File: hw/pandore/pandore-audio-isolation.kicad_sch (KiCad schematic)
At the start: 15 parts, among them U23 ISO7762, U24 ISO1640

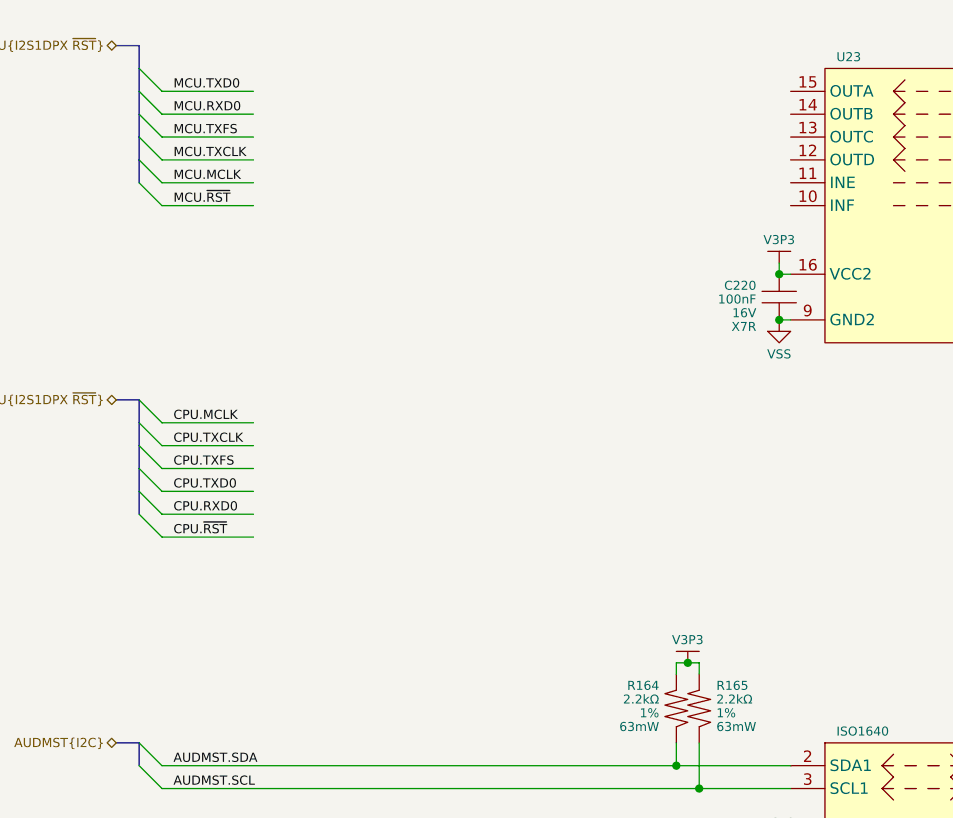
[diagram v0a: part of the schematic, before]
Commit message: lots of routing (diff, buses, power) done optimised buffer out
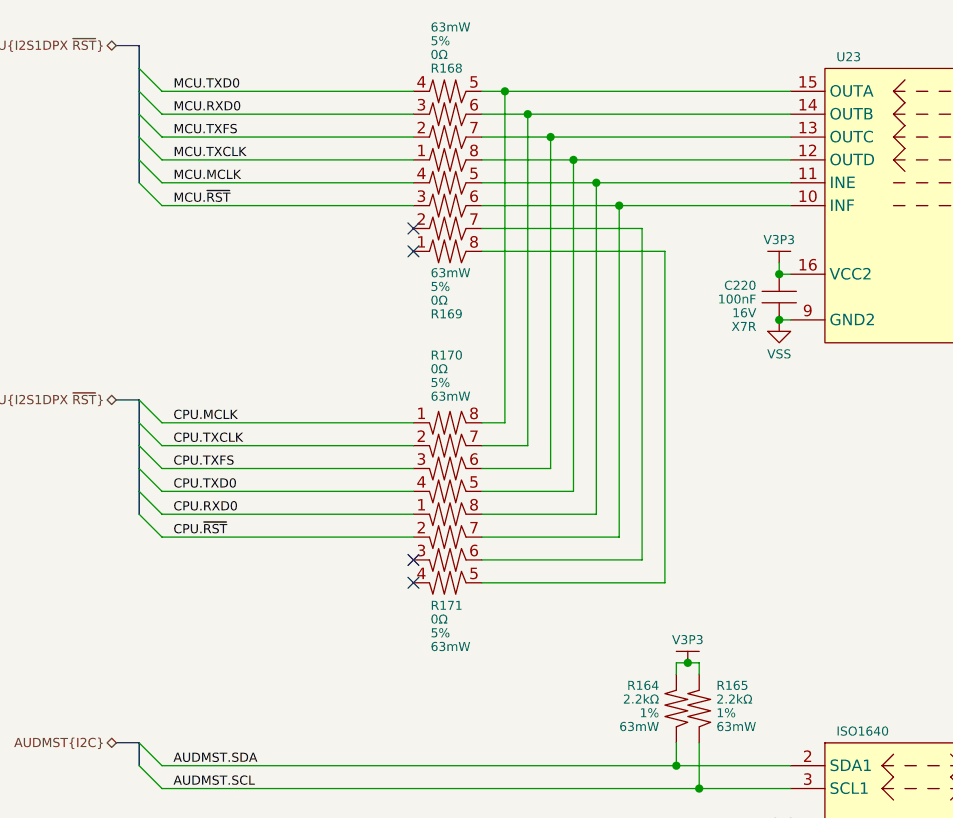
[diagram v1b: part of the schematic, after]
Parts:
- added R168, R169, R170, R171: ${Resistance}, ${Tolerance}, ${Power}, reekilib_res:RESCAXSR50P200X100X35-8, symbol reekilib_res:res_4
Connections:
- net CPU.MCLK: now also R170.1
- net CPU.RXD0: now also R171.1
- net CPU.TXCLK: now also R170.2
- net CPU.TXD0: now also R170.4
- net CPU.TXFS: now also R170.3
- net CPU.~{RST}: now also R171.2
- net MCU.MCLK: now also R169.4
- net MCU.RXD0: now also R168.3
- net MCU.TXCLK: now also R168.1
- net MCU.TXD0: now also R168.4
- net MCU.TXFS: now also R168.2
- net MCU.~{RST}: now also R169.3
- net at U23.10 (INF): now also R169.6, R171.7
- net at U23.11 (INE): now also R169.5, R171.8
- net at U23.12 (OUTD): now also R168.8, R170.5
- net at U23.13 (OUTC): now also R168.7, R170.6
- net at U23.14 (OUTB): now also R168.6, R170.7
- net at U23.15 (OUTA): now also R168.5, R170.8
- new net: R169.7, R171.6
- new net: R169.8, R171.5
- no-connect marks 0 -> 4

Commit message: added todos following review
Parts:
- R170, R171: now not fitted
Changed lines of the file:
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@@
 		(in_bom yes)
 		(on_board yes)
-		(dnp no)
+		(dnp yes)
 		(property "Reference" "R171"
 			(at 80.645 105.41 90)
@@
 		(in_bom yes)
 		(on_board yes)
-		(dnp no)
+		(dnp yes)
 		(property "Reference" "R170"
 			(at 80.645 77.597 90)

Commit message: added expansion port and more ctl to rp2350s routing much progress
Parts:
- added EXP8: I2C, reekilib_con:HDR254P1X02-TH, symbol reekilib_con:hdr-1x2
- added EXP9: I2S, reekilib_con:HDR254P1X08-TH, symbol reekilib_con:hdr-1x8
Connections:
- net AV3P3: now also EXP9.1
- net CODEC.MCLK: now also EXP9.5
- net CODEC.RXD0: now also EXP9.2
- net CODEC.SCL: now also EXP8.1
- net CODEC.SDA: now also EXP8.2
- net CODEC.TXCLK: now also EXP9.3
- net CODEC.TXD0: now also EXP9.6
- net CODEC.TXFS: now also EXP9.4
- net VSSISO: now also EXP9.8
- net ~{RST}: now also EXP9.7

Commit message: more routing/placement done added 5v load switch 1A each added second fan circuit redone all diffpair routing following new stackup calc added all (?) missing connectors to unused pins
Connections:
- net V3P3 renamed V3P3AUD
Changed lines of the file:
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@@
 	)
 	(junction
+		(at 109.22 111.76)
+		(diameter 0)
+		(color 0 0 0 0)
+	)
+	(junction
 		(at 107.95 123.19)
 		(diameter 0)
@@
 	)
 	(junction
-		(at 109.22 111.76)
-		(diameter 0)
-		(color 0 0 0 0)
-	)
-	(junction
 		(at 110.49 125.73)
 		(diameter 0)
@@
 	(wire
 		(pts
-			(xy 110.49 111.76) (xy 109.22 111.76)
+			(xy 162.56 50.8) (xy 184.15 50.8)
 		)
 		(stroke
@@
 	(wire
 		(pts
-			(xy 162.56 50.8) (xy 184.15 50.8)
+			(xy 201.93 48.26) (xy 214.63 48.26)
 		)
 		(stroke
@@
 	(wire
 		(pts
-			(xy 201.93 48.26) (xy 214.63 48.26)
+			(xy 109.22 111.76) (xy 110.49 111.76)
 		)
 		(stroke
@@
 	)
 	(symbol
+		(lib_id "reekilib_pwr:VDD")
+		(at 119.38 66.04 0)
+		(unit 1)
+		(exclude_from_sim no)
+		(in_bom no)
+		(on_board no)
+		(dnp no)
+		(property "Reference" "#PWR0243"
+			(at 119.38 62.865 0)
+			(do_not_autoplace yes)
+			(effects
+				(font
+					(size 1 1)
+				)
+				(hide yes)
+			)
+		)
+		(property "Value" "V3P3AUD"
+			(at 119.38 64.77 0)
+			(effects
+				(font
+					(size 1 1)
+				)
+			)
+		)
+		(property "Footprint" ""
+			(at 119.38 66.04 0)
+			(effects
+				(font
+					(size 1.524 1.524)
+				)
+			)
+		)
+		(property "Datasheet" ""
+			(at 119.38 66.04 0)
+			(effects
+				(font
+					(size 1.524 1.524)
+				)
+			)
+		)
+		(property "Description" ""
+			(at 119.38 66.04 0)
+			(effects
+				(font
+					(size 1.27 1.27)
+				)
+				(hide yes)
+			)
+		)
+		(pin "1"
+		)
+		(instances
+			(project "pandore"
+				(path "/e55f2700-f75a-4062-8a27-fe258faa8966/b4e2772d-7748-46ec-bd38-bc8e72cebcb8/07e56b51-9be1-414d-8c59-faa1629d64d5"
+					(reference "#PWR0243")
+					(unit 1)
+				)
+			)
+		)
+	)
+	(symbol
 		(lib_id "reekilib_cap:cap")
 		(at 119.38 135.89 0)
@@
 	)
 	(symbol
-		(lib_id "reekilib_pwr:VDD")
-		(at 119.38 130.81 0)
-		(unit 1)
-		(exclude_from_sim no)
-		(in_bom no)
-		(on_board no)
-		(dnp no)
-		(property "Reference" "#PWR0244"
-			(at 119.38 127.635 0)
-			(do_not_autoplace yes)
-			(effects
-				(font
-					(size 1 1)
-				)
-				(hide yes)
-			)
-		)
-		(property "Value" "V3P3"
-			(at 119.38 129.54 0)
-			(effects
-				(font
-					(size 1 1)
-				)
-			)
-		)
-		(property "Footprint" ""
-			(at 119.38 130.81 0)
-			(effects
-				(font
-					(size 1.524 1.524)
-				)
-			)
-		)
-		(property "Datasheet" ""
-			(at 119.38 130.81 0)
-			(effects
-				(font
-					(size 1.524 1.524)
-				)
-			)
-		)
-		(property "Description" ""
-			(at 119.38 130.81 0)
-			(effects
-				(font
-					(size 1.27 1.27)
-				)
-				(hide yes)
-			)
-		)
-		(pin "1"
-		)
-		(instances
-			(project "pandore"
-				(path "/e55f2700-f75a-4062-8a27-fe258faa8966/b4e2772d-7748-46ec-bd38-bc8e72cebcb8/07e56b51-9be1-414d-8c59-faa1629d64d5"
-					(reference "#PWR0244")
-					(unit 1)
-				)
-			)
-		)
-	)
-	(symbol
 		(lib_id "reekilib_res:res_4")
 		(at 82.55 88.9 90)
@@
 	)
 	(symbol
+		(lib_id "reekilib_pwr:VDD")
+		(at 109.22 110.49 0)
+		(unit 1)
+		(exclude_from_sim no)
+		(in_bom no)
+		(on_board no)
+		(dnp no)
+		(property "Reference" "#PWR0248"
+			(at 109.22 107.315 0)
+			(do_not_autoplace yes)
+			(effects
+				(font
+					(size 1 1)
+				)
+				(hide yes)
+			)
+		)
+		(property "Value" "V3P3AUD"
+			(at 109.22 109.22 0)
+			(effects
+				(font
+					(size 1 1)
+				)
+			)
+		)
+		(property "Footprint" ""
+			(at 109.22 110.49 0)
+			(effects
+				(font
+					(size 1.524 1.524)
+				)
+			)
+		)
+		(property "Datasheet" ""
+			(at 109.22 110.49 0)
+			(effects
+				(font
+					(size 1.524 1.524)
+				)
+			)
+		)
+		(property "Description" ""
+			(at 109.22 110.49 0)
+			(effects
+				(font
+					(size 1.27 1.27)
+				)
+				(hide yes)
+			)
+		)
+		(pin "1"
+		)
+		(instances
+			(project "pandore"
+				(path "/e55f2700-f75a-4062-8a27-fe258faa8966/b4e2772d-7748-46ec-bd38-bc8e72cebcb8/07e56b51-9be1-414d-8c59-faa1629d64d5"
+					(reference "#PWR0248")
+					(unit 1)
+				)
+			)
+		)
+	)
+	(symbol
 		(lib_id "reekilib_con:hdr-1x8")
 		(at 222.25 54.61 0)
@@
 	(symbol
 		(lib_id "reekilib_pwr:VDD")
-		(at 119.38 66.04 0)
+		(at 119.38 130.81 0)
 		(unit 1)
 		(exclude_from_sim no)
@@
 		(on_board no)
 		(dnp no)
-		(property "Reference" "#PWR0243"
-			(at 119.38 62.865 0)
+		(property "Reference" "#PWR0244"
+			(at 119.38 127.635 0)
 			(do_not_autoplace yes)
 			(effects
@@
 			)
 		)
-		(property "Value" "V3P3"
-			(at 119.38 64.77 0)
+		(property "Value" "V3P3AUD"
+			(at 119.38 129.54 0)
 			(effects
 				(font
@@
 		)
 		(property "Footprint" ""
-			(at 119.38 66.04 0)
+			(at 119.38 130.81 0)
 			(effects
 				(font
@@
 		)
 		(property "Datasheet" ""
-			(at 119.38 66.04 0)
+			(at 119.38 130.81 0)
 			(effects
 				(font
@@
 		)
 		(property "Description" ""
-			(at 119.38 66.04 0)
+			(at 119.38 130.81 0)
 			(effects
 				(font
@@
 			(project "pandore"
 				(path "/e55f2700-f75a-4062-8a27-fe258faa8966/b4e2772d-7748-46ec-bd38-bc8e72cebcb8/07e56b51-9be1-414d-8c59-faa1629d64d5"
-					(reference "#PWR0243")
+					(reference "#PWR0244")
 					(unit 1)
 				)
@@
 					(unit 1)
 				)
-			)
-		)
-	)
-	(symbol
-		(lib_id "reekilib_pwr:VDD")
-		(at 109.22 110.49 0)
-		(unit 1)
-		(exclude_from_sim no)
-		(in_bom no)
-		(on_board no)
-		(dnp no)
-		(property "Reference" "#PWR0248"
-			(at 109.22 107.315 0)
-			(do_not_autoplace yes)
-			(effects
-				(font
-					(size 1 1)
-				)
-				(hide yes)
-			)
-		)
-		(property "Value" "V3P3"
-			(at 109.22 109.22 0)
-			(effects
-				(font
-					(size 1 1)
-				)
-			)
-		)
-		(property "Footprint" ""
-			(at 109.22 110.49 0)
-			(effects
-				(font
-					(size 1.524 1.524)
-				)
-			)
-		)
-		(property "Datasheet" ""
-			(at 109.22 110.49 0)
-			(effects
-				(font
-					(size 1.524 1.524)
-				)
-			)
-		)
-		(property "Description" ""
-			(at 109.22 110.49 0)
-			(effects
-				(font
-					(size 1.27 1.27)
-				)
-				(hide yes)
-			)
-		)
-		(pin "1"
-		)
-		(instances
-			(project "pandore"
-				(path "/e55f2700-f75a-4062-8a27-fe258faa8966/b4e2772d-7748-46ec-bd38-bc8e72cebcb8/07e56b51-9be1-414d-8c59-faa1629d64d5"
-					(reference "#PWR0248")
-					(unit 1)
-				)

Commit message: finished adding mpn,mfg to all parts, finished routing placement
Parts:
- C220, C221, C222, C223: MFG2 Samsung Electro-Mechanics -> (none); MFG3 Taiyo Yuden -> (none); MPN2 CL05B104KA5NNNC -> (none); MPN3 EMK105B7104KV-F -> (none); Voltage 16V -> 25V
- EXP8: Link https://www.we-online.com/en/components/products/TBL_5_00_1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 -> (none); MFG (none) -> Adam Tech; MPN (none) -> PH1-02-UA
- EXP9: Link url-link -> (none); MFG MFG -> Amphenol ICC (FCI); MPN MPN -> 10129378-908002BLF
- R159, R160, R161, R162, R163: Link (none) -> https://yageogroup.com/products/Resistors/part/RC0402FR-074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; MFG (none) -> YAGEO; MPN (none) -> RC0402FR-0749R9L
- R164, R165, R166, R167: Link (none) -> https://yageogroup.com/products/Resistors/part/RC0402FR-072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; MFG (none) -> YAGEO; MPN (none) -> RC0402FR-072K2L
- R168, R169, R170, R171: Link (none) -> https://yageogroup.com/products/Resistors/part/YC124-JR-070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; MFG (none) -> Yageo; MPN (none) -> YC124-JR-070RL
